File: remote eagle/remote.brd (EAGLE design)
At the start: 50.8 x 50.8 mm, 13 parts, among them Y1 8MHz

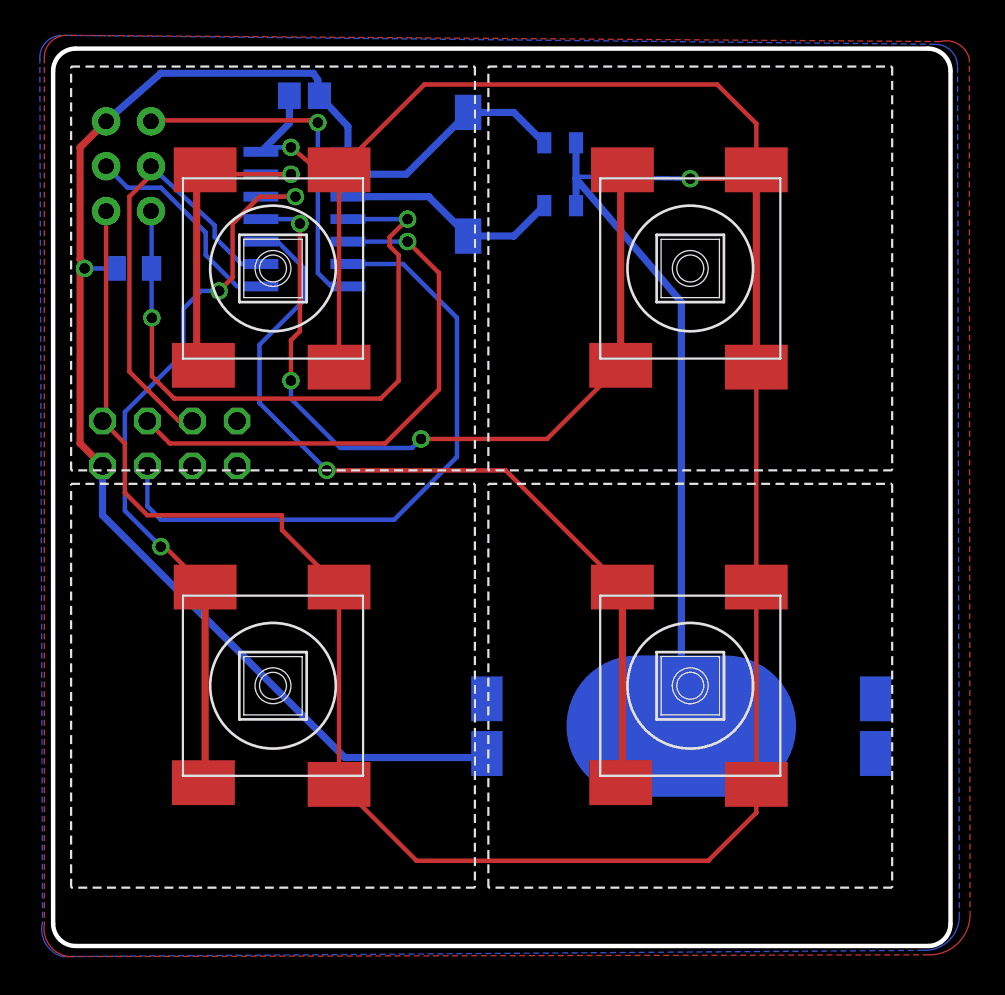
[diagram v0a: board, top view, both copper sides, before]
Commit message: New reduced size (1.44" square) board layout.
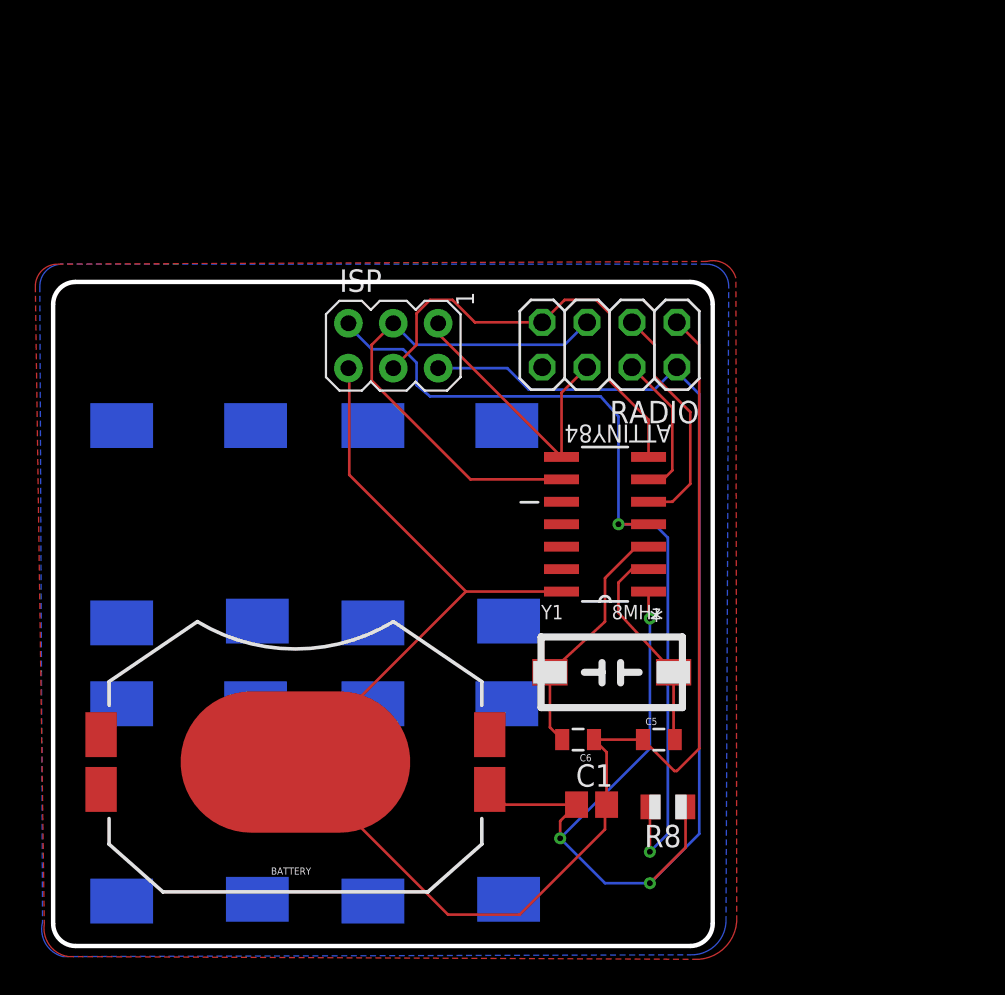
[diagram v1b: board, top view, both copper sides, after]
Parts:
- moved C1 43.3 mm to (30.5, 8.00), flipped to the top
- moved R8 42.9 mm to (34.8, 7.87), flipped to the top
- moved C5 34.2 mm to (34.3, 11.7), flipped to the top
- moved C6 30.2 mm to (29.7, 11.7), flipped to the top, turned to 180 degrees
- moved Y1 29.3 mm to (31.6, 15.5), flipped to the top, turned to 0 degrees
- moved RADIO 25.5 mm to (31.5, 34.0), flipped to the top
- moved ATTINY84 24.2 mm to (31.2, 23.9), flipped to the top, turned to 180 degrees
- moved BATTERY 21.9 mm to (13.7, 10.4), flipped to the top
- moved U$2 20.3 mm to (21.8, 23.9), flipped to the bottom
- moved ISP 18.1 mm to (19.3, 34.0), flipped to the top, turned to 270 degrees
- moved U$4 15.7 mm to (21.8, 8.13), flipped to the bottom
- moved U$1 15.3 mm to (7.62, 23.9), flipped to the bottom
- moved U$3 8.18 mm to (7.62, 8.13), flipped to the bottom
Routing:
- net GND: track 203.9 -> 94.9 mm, vias 2 -> 0
- net BUTTON4: track 47.7 -> 0.00 mm, vias 1 -> 0
- net BUTTON2: track 45.3 -> 0.00 mm, vias 3 -> 0
- net BUTTON3: track 43.0 -> 0.00 mm, vias 3 -> 0
- net CSN: track 36.9 -> 8.35 mm
- net BUTTON1: track 18.6 -> 0.00 mm, vias 1 -> 0
- net CE: track 30.8 -> 13.3 mm, vias 1 -> 0
- net MOSI: track 11.0 -> 25.3 mm
- net RESET: track 37.4 -> 50.0 mm
- net VCC: track 71.4 -> 80.4 mm, vias 1 -> 3
- net MISO: track 19.1 -> 16.1 mm, vias 1 -> 0
- net SCK: track 25.9 -> 28.8 mm
- net XTL2: track 12.8 -> 14.0 mm
- net XTL1: track 13.3 -> 12.2 mm
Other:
- board size 50.8 x 50.8 mm -> 37.3 x 37.6 mm
- board text added: "Turn Touch Remote 3 April 2014 - Rev. 4"
- board text removed: "Turn Touch Remote 13 March 2014 - Rev. 3"

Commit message: Resizing board to accomodate new tactile switches. Sending to printer.
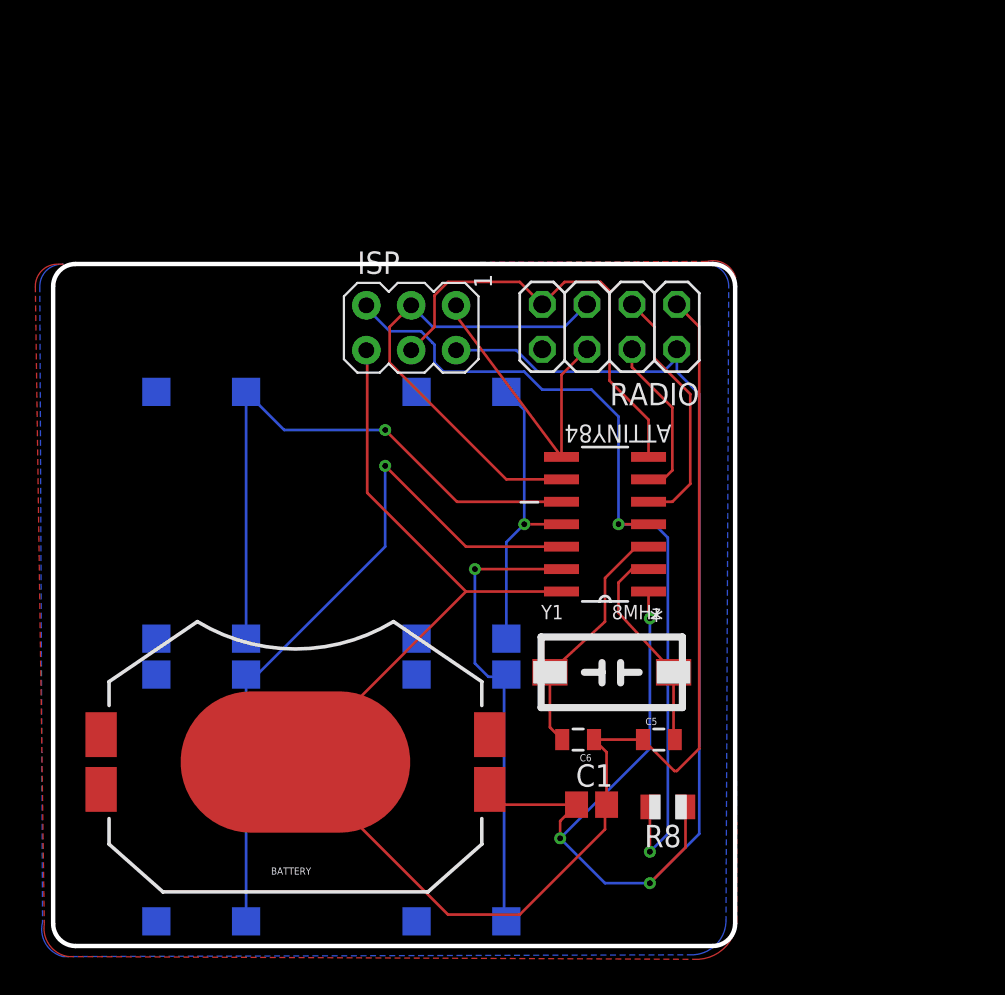
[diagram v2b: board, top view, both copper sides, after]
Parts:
- U$1, U$2, U$3, U$4: value 5GSH9 -> TL3300SMD; device remote:5GSH9 -> remote:TL3300
- moved U$1 21.9 mm to (23.1, 8.38)
- moved U$4 21.1 mm to (8.38, 24.4)
- moved ISP 1.44 mm to (20.3, 35.0)
- moved U$2 1.37 mm to (23.1, 24.4)
- moved RADIO 1.02 mm to (31.5, 35.1)
- moved U$3 0.80 mm to (8.38, 8.38)
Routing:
- net BUTTON3: track 0.00 -> 41.4 mm, vias 0 -> 1
- net BUTTON4: track 0.00 -> 34.4 mm, vias 0 -> 1
- net BUTTON1: track 0.00 -> 26.3 mm, vias 0 -> 1
- net BUTTON2: track 0.00 -> 16.9 mm, vias 0 -> 1
- net GND: track 94.9 -> 96.5 mm
- net SCK: track 28.8 -> 27.2 mm
- net MISO: track 16.1 -> 17.3 mm
- net CE: track 13.3 -> 14.3 mm
- net CSN: track 8.35 -> 9.36 mm
- net RESET: track 50.0 -> 49.2 mm
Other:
- board size 37.3 x 37.6 mm -> 38.6 x 38.6 mm

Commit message: Fixing up board.
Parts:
- moved ISP 11.9 mm to (8.33, 35.0)
- moved BATTERY 1.27 mm to (12.4, 10.4)
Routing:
- net SCK: track 27.2 -> 51.2 mm
- net VCC: track 80.7 -> 93.7 mm
- net RESET: track 49.2 -> 61.2 mm
- net MOSI: track 25.4 -> 37.4 mm
- net MISO: track 17.3 -> 28.8 mm
- net GND: track 96.5 -> 105.0 mm
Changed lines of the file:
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@@
 </element>
 <element name="C1" library="adafruit" package="C0805" value=".1uf" x="30.48" y="8.001"/>
-<element name="ISP" library="adafruit" package="AVRISP" value="AVRISP-6" x="20.27" y="34.998" rot="R270"/>
+<element name="ISP" library="adafruit" package="AVRISP" value="AVRISP-6" x="8.332" y="34.998" rot="R270"/>
 <element name="RADIO" library="pinhead" package="2X04" value="NRF24L01" x="31.496" y="35.052" rot="R180"/>
 <element name="R8" library="adafruit" package="R0805" value="10k" x="34.798" y="7.874" rot="R180"/>
 <element name="Y1" library="remote" package="NX8045GB" value="8MHz" x="31.623" y="15.494"/>
-<element name="BATTERY" library="SparkFun-Electromechanical" package="BATTCON_20MM_4LEGS_OVERPASTE" value="CR2032" x="13.716" y="10.414" rot="R180"/>
+<element name="BATTERY" library="SparkFun-Electromechanical" package="BATTCON_20MM_4LEGS_OVERPASTE" value="CR2032" x="12.446" y="10.414" rot="R180"/>
 <element name="C5" library="SparkFun-Passives" package="0805" value="15pF" x="34.29" y="11.684"/>
 <element name="C6" library="SparkFun-Passives" package="0805" value="15pF" x="29.718" y="11.684" rot="R180"/>
@@
 <contactref element="U$4" pad="P$1"/>
 <contactref element="U$4" pad="P$2"/>
-<wire x1="13.716" y1="10.414" x2="22.352" y2="1.778" width="0.1524" layer="1"/>
-<wire x1="22.352" y1="1.778" x2="26.416" y2="1.778" width="0.1524" layer="1"/>
+<wire x1="12.446" y1="10.414" x2="21.082" y2="1.778" width="0.1524" layer="1"/>
+<wire x1="21.082" y1="1.778" x2="26.416" y2="1.778" width="0.1524" layer="1"/>
 <wire x1="26.416" y1="1.778" x2="31.242" y2="6.604" width="0.1524" layer="1"/>
 <wire x1="31.242" y1="6.604" x2="31.242" y2="7.913" width="0.1524" layer="1"/>
@@
 <wire x1="31.33" y1="10.972" x2="30.618" y2="11.684" width="0.1524" layer="1"/>
 <wire x1="30.618" y1="11.684" x2="33.39" y2="11.684" width="0.1524" layer="1"/>
-<wire x1="23.368" y1="20.066" x2="13.716" y2="10.414" width="0.1524" layer="1"/>
-<wire x1="28.7782" y1="20.066" x2="23.368" y2="20.066" width="0.1524" layer="1"/>
-<wire x1="23.368" y1="20.066" x2="17.78" y2="25.654" width="0.1524" layer="1"/>
-<wire x1="17.78" y1="25.654" x2="17.78" y2="33.678" width="0.1524" layer="1"/>
-<wire x1="17.78" y1="33.678" x2="17.73" y2="33.728" width="0.1524" layer="1"/>
+<wire x1="22.098" y1="20.066" x2="12.446" y2="10.414" width="0.1524" layer="1"/>
+<wire x1="28.7782" y1="20.066" x2="22.098" y2="20.066" width="0.1524" layer="1"/>
+<wire x1="22.098" y1="20.066" x2="16.51" y2="25.654" width="0.1524" layer="1"/>
+<wire x1="5.842" y1="33.678" x2="5.792" y2="33.728" width="0.1524" layer="1"/>
 <wire x1="35.306" y1="36.322" x2="36.576" y2="35.052" width="0.1524" layer="1"/>
 <wire x1="36.576" y1="35.052" x2="36.576" y2="11.176" width="0.1524" layer="1"/>
@@
 <wire x1="35.306" y1="9.906" x2="35.168" y2="9.906" width="0.1524" layer="1"/>
 <wire x1="35.168" y1="9.906" x2="33.39" y2="11.684" width="0.1524" layer="1"/>
+<wire x1="16.51" y1="25.654" x2="13.866" y2="25.654" width="0.1524" layer="1"/>
+<wire x1="13.866" y1="25.654" x2="5.792" y2="33.728" width="0.1524" layer="1"/>
+<wire x1="16.51" y1="25.654" x2="20.574" y2="31.369" width="0" layer="19" extent="1-16"/>
+<wire x1="20.574" y1="1.397" x2="21.082" y2="1.778" width="0" layer="19" extent="1-16"/>
+<wire x1="5.842" y1="31.369" x2="5.842" y2="33.678" width="0" layer="19" extent="1-16"/>
+<wire x1="20.574" y1="17.399" x2="22.098" y2="20.066" width="0" layer="19" extent="1-16"/>
+<wire x1="20.574" y1="15.367" x2="20.574" y2="17.399" width="0" layer="19" extent="16-16"/>
+<wire x1="5.842" y1="15.367" x2="12.446" y2="10.414" width="0" layer="19" extent="1-16"/>
+<wire x1="5.842" y1="17.399" x2="5.842" y2="15.367" width="0" layer="19" extent="16-16"/>
+<wire x1="5.842" y1="1.397" x2="12.446" y2="10.414" width="0" layer="19" extent="1-16"/>
 </signal>
 <signal name="MISO">
@@
 <wire x1="28.7782" y1="27.686" x2="28.7782" y2="32.3342" width="0.1524" layer="1"/>
 <wire x1="28.7782" y1="32.3342" x2="30.226" y2="33.782" width="0.1524" layer="1"/>
-<wire x1="22.81" y1="36.268" x2="22.81" y2="35.6862" width="0.1524" layer="1"/>
-<wire x1="22.81" y1="35.6862" x2="28.7782" y2="27.686" width="0.1524" layer="1"/>
+<wire x1="10.872" y1="36.268" x2="10.872" y2="35.6862" width="0.1524" layer="1"/>
+<wire x1="28.7782" y1="27.686" x2="26.416" y2="27.686" width="0.1524" layer="1"/>
+<wire x1="26.416" y1="27.686" x2="17.78" y2="36.322" width="0.1524" layer="1"/>
+<wire x1="17.78" y1="36.322" x2="10.926" y2="36.322" width="0.1524" layer="1"/>
+<wire x1="10.926" y1="36.322" x2="10.872" y2="36.268" width="0.1524" layer="1"/>
 </signal>
 <signal name="MOSI">
@@
 <wire x1="33.7058" y1="29.7942" x2="31.496" y2="32.004" width="0.1524" layer="1"/>
 <wire x1="31.496" y1="32.004" x2="31.496" y2="37.084" width="0.1524" layer="1"/>
-<wire x1="22.352" y1="37.592" x2="21.59" y2="36.83" width="0.1524" layer="1"/>
-<wire x1="21.59" y1="36.83" x2="21.59" y2="35.048" width="0.1524" layer="1"/>
-<wire x1="21.59" y1="35.048" x2="20.27" y2="33.728" width="0.1524" layer="1"/>
+<wire x1="10.414" y1="37.592" x2="9.652" y2="36.83" width="0.1524" layer="1"/>
+<wire x1="9.652" y1="36.83" x2="9.652" y2="35.048" width="0.1524" layer="1"/>
+<wire x1="9.652" y1="35.048" x2="8.332" y2="33.728" width="0.1524" layer="1"/>
 <wire x1="31.496" y1="37.084" x2="30.988" y2="37.592" width="0.1524" layer="1"/>
 <wire x1="30.988" y1="37.592" x2="28.956" y2="37.592" width="0.1524" layer="1"/>
 <wire x1="28.956" y1="37.592" x2="27.686" y2="36.322" width="0.1524" layer="1"/>
 <wire x1="27.686" y1="36.322" x2="26.416" y2="37.592" width="0.1524" layer="1"/>
-<wire x1="26.416" y1="37.592" x2="22.352" y2="37.592" width="0.1524" layer="1"/>
+<wire x1="26.416" y1="37.592" x2="10.414" y2="37.592" width="0.1524" layer="1"/>
 </signal>
 <signal name="SCK">
@@
 <contactref element="ISP" pad="3"/>
 <contactref element="RADIO" pad="5"/>
-<wire x1="28.7782" y1="26.416" x2="25.654" y2="26.416" width="0.1524" layer="1"/>
-<wire x1="25.654" y1="26.416" x2="19.05" y2="33.02" width="0.1524" layer="1"/>
-<wire x1="19.05" y1="33.02" x2="19.05" y2="35.048" width="0.1524" layer="1"/>
-<wire x1="19.05" y1="35.048" x2="20.27" y2="36.268" width="0.1524" layer="1"/>
+<wire x1="28.7782" y1="26.416" x2="25.4" y2="26.416" width="0.1524" layer="1"/>
+<wire x1="7.112" y1="33.02" x2="7.112" y2="35.048" width="0.1524" layer="1"/>
+<wire x1="7.112" y1="35.048" x2="8.332" y2="36.268" width="0.1524" layer="1"/>
 <wire x1="30.226" y1="36.322" x2="28.956" y2="35.052" width="0.1524" layer="16"/>
-<wire x1="28.956" y1="35.052" x2="21.486" y2="35.052" width="0.1524" layer="16"/>
-<wire x1="21.486" y1="35.052" x2="20.27" y2="36.268" width="0.1524" layer="16"/>
+<wire x1="28.956" y1="35.052" x2="9.548" y2="35.052" width="0.1524" layer="16"/>
+<wire x1="9.548" y1="35.052" x2="8.332" y2="36.268" width="0.1524" layer="16"/>
+<wire x1="25.4" y1="26.416" x2="16.764" y2="35.052" width="0.1524" layer="1"/>
+<wire x1="16.764" y1="35.052" x2="9.548" y2="35.052" width="0.1524" layer="1"/>
+<wire x1="9.548" y1="35.052" x2="8.332" y2="36.268" width="0.1524" layer="1"/>
 </signal>
 <signal name="BUTTON1">
@@
 <contactref element="BATTERY" pad="1"/>
 <wire x1="29.63" y1="8.001" x2="25.579" y2="8.001" width="0.1524" layer="1"/>
-<wire x1="25.579" y1="8.001" x2="24.716" y2="8.864" width="0.1524" layer="1"/>
+<wire x1="25.579" y1="8.001" x2="23.446" y2="8.864" width="0.1524" layer="1"/>
 <wire x1="35.798" y1="7.874" x2="35.798" y2="5.572" width="0.1524" layer="1"/>
 <wire x1="35.798" y1="5.572" x2="33.782" y2="3.556" width="0.1524" layer="1"/>
@@
 <wire x1="36.576" y1="31.242" x2="36.576" y2="6.35" width="0.1524" layer="16"/>
 <wire x1="36.576" y1="6.35" x2="33.782" y2="3.556" width="0.1524" layer="16"/>
-<wire x1="22.81" y1="33.728" x2="26.216" y2="33.728" width="0.1524" layer="16"/>
+<wire x1="10.872" y1="33.728" x2="26.216" y2="33.728" width="0.1524" layer="16"/>
 <wire x1="26.216" y1="33.728" x2="27.432" y2="32.512" width="0.1524" layer="16"/>
 <wire x1="27.432" y1="32.512" x2="34.544" y2="32.512" width="0.1524" layer="16"/>
@@
 <wire x1="33.782" y1="5.334" x2="33.782" y2="7.858" width="0.1524" layer="1"/>
 <wire x1="33.782" y1="7.858" x2="33.798" y2="7.874" width="0.1524" layer="1"/>
-<wire x1="17.73" y1="36.268" x2="17.73" y2="36.118" width="0.1524" layer="16"/>
-<wire x1="17.73" y1="36.118" x2="19.05" y2="34.798" width="0.1524" layer="16"/>
-<wire x1="19.05" y1="34.798" x2="20.828" y2="34.798" width="0.1524" layer="16"/>
-<wire x1="20.828" y1="34.798" x2="21.463" y2="34.163" width="0.1524" layer="16"/>
+<wire x1="5.792" y1="36.268" x2="5.792" y2="36.118" width="0.1524" layer="16"/>
+<wire x1="5.792" y1="36.118" x2="7.112" y2="34.798" width="0.1524" layer="16"/>
+<wire x1="7.112" y1="34.798" x2="8.89" y2="34.798" width="0.1524" layer="16"/>
+<wire x1="8.89" y1="34.798" x2="9.652" y2="34.036" width="0.1524" layer="16"/>
 <wire x1="32.004" y1="29.972" x2="32.004" y2="23.876" width="0.1524" layer="16"/>
 <wire x1="32.004" y1="29.972" x2="30.48" y2="31.496" width="0.1524" layer="16"/>
 <wire x1="30.48" y1="31.496" x2="27.686" y2="31.496" width="0.1524" layer="16"/>
 <wire x1="27.686" y1="31.496" x2="26.67" y2="32.512" width="0.1524" layer="16"/>
-<wire x1="26.67" y1="32.512" x2="22.098" y2="32.512" width="0.1524" layer="16"/>
-<wire x1="22.098" y1="32.512" x2="21.59" y2="33.02" width="0.1524" layer="16"/>
-<wire x1="21.59" y1="33.02" x2="21.59" y2="34.036" width="0.1524" layer="16"/>
-<wire x1="21.59" y1="34.036" x2="21.463" y2="34.163" width="0.1524" layer="16"/>
+<wire x1="26.67" y1="32.512" x2="10.16" y2="32.512" width="0.1524" layer="16"/>
+<wire x1="10.16" y1="32.512" x2="9.652" y2="33.02" width="0.1524" layer="16"/>
+<wire x1="9.652" y1="33.02" x2="9.652" y2="34.036" width="0.1524" layer="16"/>
 </signal>
 <signal name="CE">

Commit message: Rev. 5, includes new isp touch.
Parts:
- removed ISP: AVRISP-6, adafruit:AVRISP
- added J1: ISP Touch, remote:AVX_9188_6-WAY_MATING_GUIDE
- moved RADIO 0.76 mm to (32.3, 35.1)
- turned U$2 to 180 degrees
- turned U$3 to 180 degrees
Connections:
- net GND: now also J1.6; no longer ISP.6
- net MISO: now also J1.1; no longer ISP.1
- net MOSI: now also J1.4; no longer ISP.4
- net RESET: now also J1.5; no longer ISP.5
- net SCK: now also J1.3; no longer ISP.3
- net VCC: now also J1.2; no longer ISP.2
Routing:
- net GND: track 105.0 -> 169.2 mm, vias 0 -> 3
- net RESET: track 61.2 -> 86.6 mm
- net SCK: track 51.2 -> 38.9 mm, vias 0 -> 1
- net VCC: track 93.7 -> 102.0 mm, vias 3 -> 4
- net BUTTON2: track 16.9 -> 23.8 mm
- net BUTTON3: track 41.4 -> 34.5 mm
- net MISO: track 28.8 -> 25.5 mm
- net MOSI: track 37.4 -> 36.7 mm
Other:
- board text added: "Turn Touch Remote 5 May 2014 - Rev. 5"
- board text removed: "Turn Touch Remote 3 April 2014 - Rev. 4"
